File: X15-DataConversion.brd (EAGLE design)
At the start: 24.3 x 25.4 mm, 26 parts, among them Y1 ECS-80-18-4X

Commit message: alumni review changes
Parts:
- removed D1: Green, SparkFun-LED:LED-0603
- removed D3: Orange, SparkFun-LED:LED-0603
- added LED1, LED2: LSM0805452VLED_05452V_VCC, X15-Data-Conversion-Parts:LED_05452V_VCC
- moved R6 0.25 mm to (6.38, 15.4)
- moved R7 0.24 mm to (4.90, 15.4)
- moved U$1 0.09 mm to (8.84, 21.4)
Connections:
- net GND: now also LED1.2, LED2.2; no longer D1.C, D3.C
- net N$1: now also LED1.1; no longer D3.A
- net N$11: now also LED2.1; no longer D1.A
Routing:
- net GND: track 2.83 -> 19.1 mm, vias 6 -> 8
- net 3V3: track 62.8 -> 63.5 mm

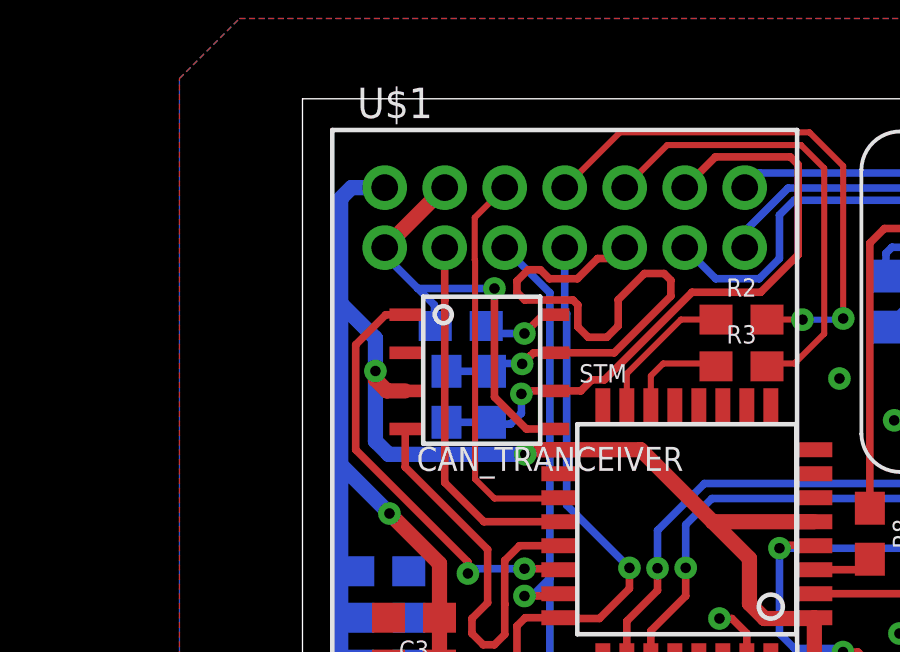
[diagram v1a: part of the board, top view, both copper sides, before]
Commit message: fixed drc error
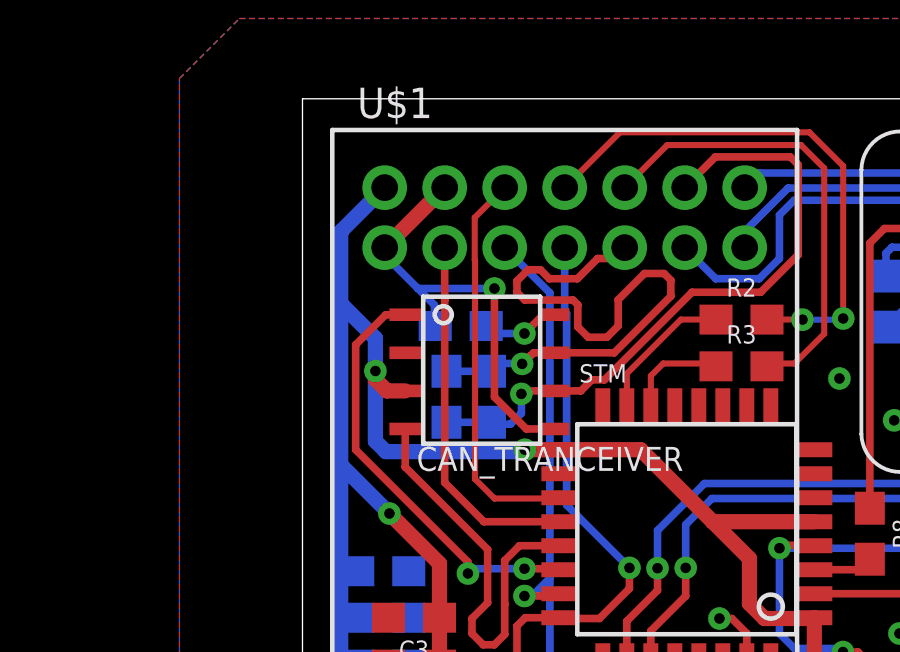
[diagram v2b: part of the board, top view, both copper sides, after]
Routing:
- net 3V3: track 63.5 -> 62.8 mm
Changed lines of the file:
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@@
 <wire x1="8.663" y1="13.626" x2="11.374" y2="13.626" width="0.508" layer="1"/>
 <wire x1="13.774" y1="11.226" x2="17.163" y2="11.226" width="0.508" layer="1"/>
-<via x="7.52749375" y="13.47250625" extent="1-16" drill="0.35"/>
+<via x="7.51479375" y="13.62490625" extent="1-16" drill="0.35"/>
 <wire x1="17.163" y1="8.026" x2="17.163" y2="5.25325" width="0.508" layer="1"/>
 <wire x1="17.415" y1="5.00125" x2="17.163" y2="5.25325" width="0.508" layer="1"/>
-<wire x1="7.52749375" y1="13.47250625" x2="7.6809875" y2="13.626" width="0.508" layer="1"/>
-<wire x1="7.6809875" y1="13.626" x2="8.663" y2="13.626" width="0.508" layer="1"/>
+<wire x1="7.51479375" y1="13.62490625" x2="7.5158875" y2="13.626" width="0.508" layer="1"/>
+<wire x1="7.5158875" y1="13.626" x2="8.663" y2="13.626" width="0.508" layer="1"/>
 <wire x1="1.375" y1="9.5" x2="1.375" y2="8.125" width="0.508" layer="16"/>
 <wire x1="1.375" y1="8.125" x2="1.375" y2="6.625" width="0.508" layer="16"/>
@@
 <via x="3" y="11.5" extent="1-16" drill="0.35"/>
 <wire x1="3" y1="11.5" x2="1.375" y2="13.125" width="0.508" layer="16"/>
-<wire x1="1.375" y1="13.125" x2="1.375" y2="18.5" width="0.508" layer="16"/>
-<wire x1="1.3741375" y1="22.0025375" x2="1.3741375" y2="18.5008625" width="0.508" layer="16"/>
 <wire x1="17.163" y1="8.026" x2="17.137" y2="8" width="0.508" layer="1"/>
 <wire x1="17.137" y1="8" x2="15.5" y2="8" width="0.508" layer="1"/>
@@
 <wire x1="15" y1="8.5" x2="15" y2="10" width="0.508" layer="1"/>
 <wire x1="15" y1="10" x2="13.774" y2="11.226" width="0.508" layer="1"/>
-<wire x1="7.52749375" y1="13.47250625" x2="2.97250625" y2="13.47250625" width="0.508" layer="16"/>
+<wire x1="7.51479375" y1="13.62490625" x2="7.45129375" y2="13.56140625" width="0.508" layer="16"/>
+<wire x1="7.45129375" y1="13.56140625" x2="2.88360625" y2="13.56140625" width="0.508" layer="16"/>
 <wire x1="2.5326" y1="16.25" x2="2.5326" y2="17.3424" width="0.508" layer="16"/>
-<wire x1="2.5326" y1="17.3424" x2="1.375" y2="18.5" width="0.508" layer="16"/>
-<wire x1="1.375" y1="18.5" x2="1.3741375" y2="18.5008625" width="0.508" layer="16"/>
 <wire x1="2.5326" y1="15.9674" x2="2.5326" y2="16.25" width="0.508" layer="1"/>
 <via x="2.5326" y="16.25" extent="1-16" drill="0.35"/>
-<wire x1="2.97250625" y1="13.47250625" x2="2.5326" y2="13.9124125" width="0.508" layer="16"/>
+<wire x1="2.88360625" y1="13.56140625" x2="2.5326" y2="13.9124125" width="0.508" layer="16"/>
 <wire x1="2.5326" y1="13.9124125" x2="2.5326" y2="16.25" width="0.508" layer="16"/>
 <wire x1="3.525" y1="15.587" x2="2.913" y2="15.587" width="0.508" layer="1"/>
 <wire x1="2.913" y1="15.587" x2="2.5326" y2="15.9674" width="0.508" layer="1"/>
-<wire x1="2.8419" y1="22.3627" x2="1.7343" y2="22.3627" width="0.508" layer="16"/>
-<wire x1="1.7343" y1="22.3627" x2="1.3741375" y2="22.0025375" width="0.508" layer="16"/>
+<wire x1="2.8419" y1="22.3627" x2="1.375" y2="20.8958" width="0.508" layer="16"/>
+<wire x1="1.375" y1="20.8958" x2="1.375" y2="18.5" width="0.508" layer="16"/>
+<wire x1="1.375" y1="18.5" x2="1.375" y2="13.125" width="0.508" layer="16"/>
+<wire x1="2.5326" y1="17.3424" x2="1.375" y2="18.5" width="0.508" layer="16"/>
 </signal>
 <signal name="ALERT1">

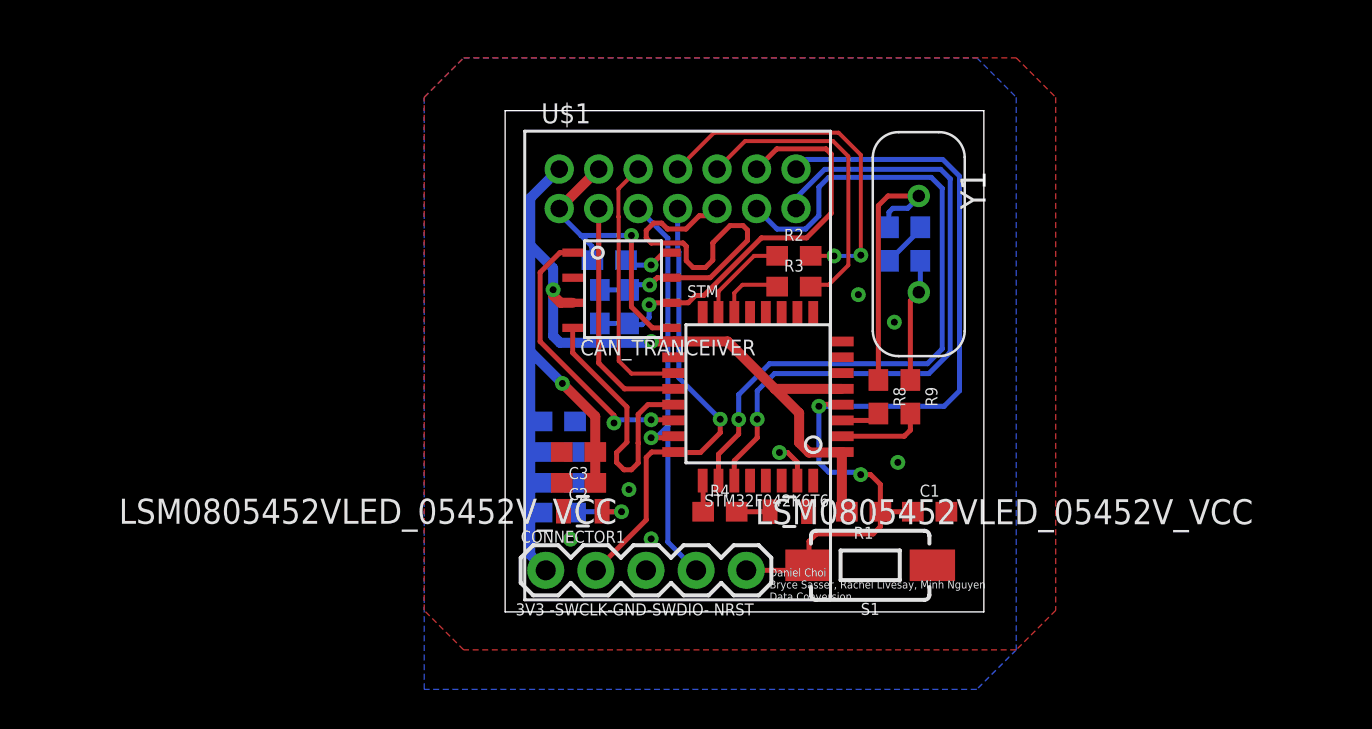
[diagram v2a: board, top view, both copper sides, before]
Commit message: removed oscillator and fixed trace widths
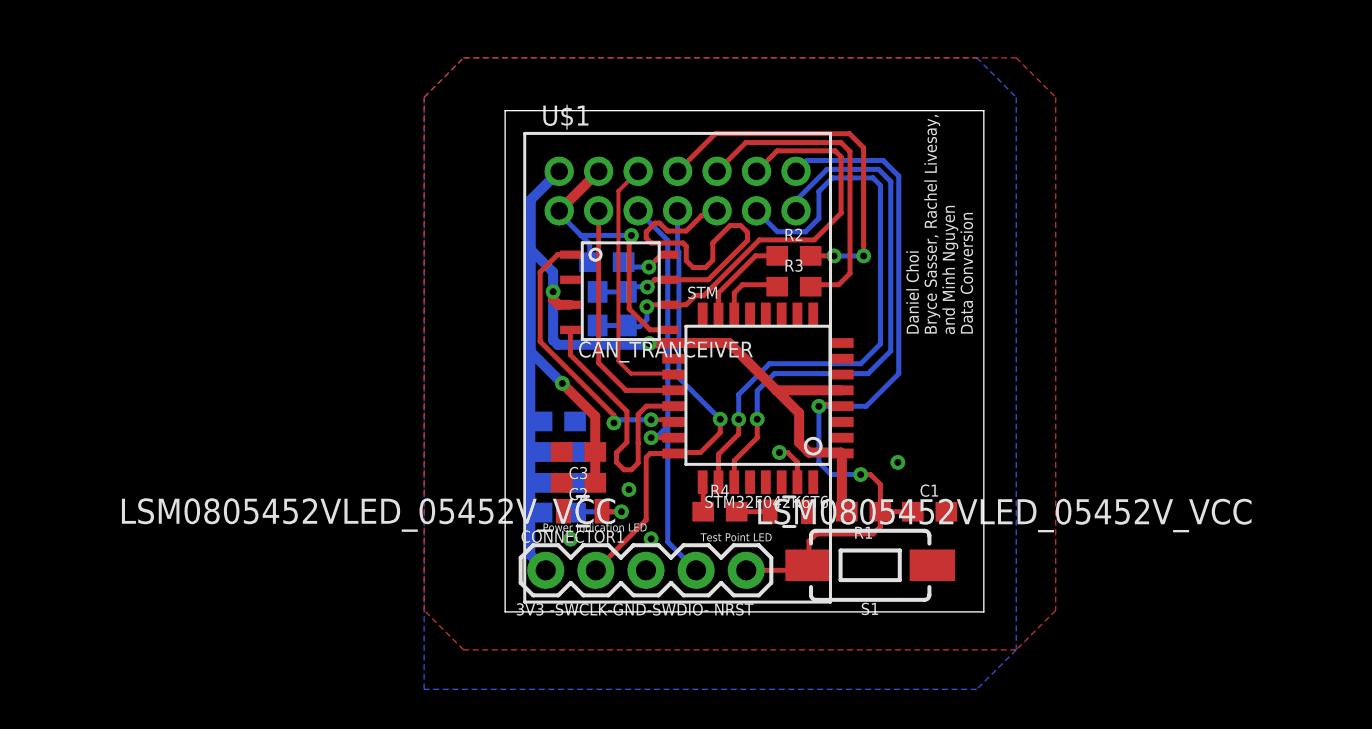
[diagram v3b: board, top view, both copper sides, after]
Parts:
- removed C7, C8: 18pF, SparkFun-RF:0603
- removed R8, R9: 0, SparkFun-Resistors:0603
- removed Y1: ECS-80-18-4X, X15-Data-Conversion-Parts:XTAL_ECS-80-18-4X
- moved R10 0.15 mm to (5.26, 17.6)
- moved R6 0.15 mm to (6.27, 15.3)
- moved R7 0.15 mm to (4.79, 15.3)
- moved CAN_TRANCEIVER 0.15 mm to (3.41, 18.0)
- moved U$1 0.11 mm to (8.84, 21.2)
- moved STM 0.08 mm to (15.7, 15.0)
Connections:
- removed net N$3: C7.1, R8.1, Y1.1
- removed net N$4: C8.1, R9.1, Y1.2
- net GND: no longer C7.2, C8.2
- net OSC_IN: no longer R9.2
- net OSC_OUT: no longer R8.2
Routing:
- net N$3: track 13.7 -> 0.00 mm
- net NRST: track 47.0 -> 40.4 mm
- net N$4: track 6.25 -> 0.00 mm
- net ALERT2: track 36.2 -> 30.0 mm
- net ALERT1: track 33.6 -> 27.5 mm
- net OSC_IN: track 4.44 -> 0.00 mm
- net GND: track 19.1 -> 16.9 mm, vias 8 -> 6
- net OSC_OUT: track 2.00 -> 0.00 mm
- net CAN_L: track 21.9 -> 22.9 mm
- net C2_1: track 15.4 -> 16.0 mm
- net C2_2: track 18.2 -> 18.7 mm
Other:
- board text added: "Daniel Choi Bryce Sasser, Rachel Livesay, and Minh Nguyen Data Conversion"
- board text added: "Power Indication LED"
- board text added: "Test Point LED"
- board text removed: "Daniel Choi Bryce Sasser, Rachel Livesay, Minh Nguyen Data Conversion"

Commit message: added 5 pin connector
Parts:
- added U$2: STM_CONN, X15-Data-Conversion-Parts:1X05
- moved R3 0.10 mm to (14.7, 16.5), flipped to the bottom, turned to 180 degrees
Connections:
- new net ADC_IN0: STM.PA5, U$2.1
- new net ADC_IN1: STM.PA4, U$2.2
- new net ADC_IN2: STM.PA6, U$2.3
- net 3V3: now also U$2.4
- net GND: now also U$2.5
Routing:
- net ADC_IN2: track 0.00 -> 10.8 mm
- net ADC_IN0: track 0.00 -> 9.61 mm
- net ADC_IN1: track 0.00 -> 8.30 mm
- net 3V3: track 62.4 -> 67.8 mm
- net C2_1: track 16.0 -> 15.8 mm, vias 0 -> 1
- net N$7: vias 0 -> 1
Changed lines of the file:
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@@
 <wire x1="24.3586" y1="25.3238" x2="0.1016" y2="25.3238" width="0" layer="20"/>
 <wire x1="0.1016" y1="25.3238" x2="0.1016" y2="-0.0762" width="0" layer="20"/>
-<text x="23.8031" y="13.9525" size="0.6096" layer="21" rot="R90">Daniel Choi
-Bryce Sasser, Rachel Livesay,
+<text x="23.8031" y="18.9525" size="0.508" layer="21" rot="R90">Daniel Choi
+Bryce Sasser,
+Rachel Livesay,
 and Minh Nguyen
 Data Conversion</text>
@@
 <attribute name="VALUE" x="14.515" y="17.203" size="0.6096" layer="28" font="vector" ratio="20" rot="MR0" align="top-center"/>
 </element>
-<element name="R3" library="SparkFun-Resistors" package="0603" value="4.7k" x="14.735" y="16.405" smashed="yes">
-<attribute name="NAME" x="14.735" y="17.167" size="0.6096" layer="25" font="vector" ratio="20" align="bottom-center"/>
-<attribute name="PROD_ID" value=" " x="14.735" y="16.405" size="1.778" layer="27" display="off"/>
-<attribute name="VALUE" x="14.735" y="15.643" size="0.6096" layer="27" font="vector" ratio="20" align="top-center"/>
+<element name="R3" library="SparkFun-Resistors" package="0603" value="4.7k" x="14.7223" y="16.5007" smashed="yes" rot="MR180">
+<attribute name="NAME" x="14.7223" y="15.7387" size="0.6096" layer="26" font="vector" ratio="20" rot="MR180" align="bottom-center"/>
+<attribute name="PROD_ID" value=" " x="14.7223" y="16.5007" size="1.778" layer="28" rot="MR180" display="off"/>
+<attribute name="VALUE" x="14.7223" y="17.2627" size="0.6096" layer="28" font="vector" ratio="20" rot="MR180" align="top-center"/>
 </element>
 <element name="R4" library="SparkFun-Resistors" package="0603" value="470" x="10.985" y="5.00125" smashed="yes">
@@
 <attribute name="PROD_ID" value=" " x="4.788" y="15.2886" size="1.778" layer="28" rot="MR90" display="off"/>
 <attribute name="VALUE" x="4.026" y="15.2886" size="0.6096" layer="28" font="vector" ratio="20" rot="MR90" align="top-center"/>
+</element>
+<element name="U$2" library="X15-Data-Conversion-Parts" package="1X05" package3d_urn="urn:adsk.eagle:package:38192072/1" value="STM_CONN" x="22.012" y="17.6251" smashed="yes" rot="R270">
+<attribute name="NAME" x="23.409" y="18.8951" size="0.6096" layer="25" font="vector" ratio="20" rot="R270"/>
+<attribute name="VALUE" x="19.726" y="19.1491" size="0.6096" layer="25" rot="R270"/>
 </element>
 </elements>
@@
 <wire x1="3.9489" y1="19" x2="6.5" y2="19" width="0.254" layer="16"/>
 <via x="6.5" y="19" extent="1-16" drill="0.35"/>
-<wire x1="6.5" y1="19" x2="6.3857" y2="18.8857" width="0.254" layer="1"/>
-<wire x1="6.3857" y1="18.8857" x2="6.3857" y2="15.2805" width="0.254" layer="1"/>
+<wire x1="6.5" y1="19" x2="6.5" y2="15.1662" width="0.254" layer="1"/>
 <wire x1="7.4508" y1="14.2154" x2="8.3607" y2="14.2154" width="0.254" layer="1"/>
 <wire x1="2.8419" y1="20.107" x2="3.9489" y2="19" width="0.254" layer="16"/>
-<wire x1="6.3857" y1="15.2805" x2="7.4508" y2="14.2154" width="0.254" layer="1"/>
+<wire x1="6.5" y1="15.1662" x2="7.4508" y2="14.2154" width="0.254" layer="1"/>
 <wire x1="4.3857" y1="18.5632" x2="3.9489" y2="19" width="0.254" layer="16"/>
 <wire x1="4.3857" y1="17.6734" x2="4.3857" y2="18.5632" width="0.254" layer="16"/>
+<contactref element="U$2" pad="5"/>
 </signal>
 <signal name="NRST">
@@
 <contactref element="STM" pad="PB0"/>
 <contactref element="R3" pad="1"/>
-<wire x1="13.885" y1="16.405" x2="13.79" y2="16.5" width="0.2032" layer="1"/>
-<wire x1="13.79" y1="16.5" x2="12.125" y2="16.5" width="0.254" layer="1"/>
+<wire x1="13.79" y1="16.5" x2="13.8723" y2="16.5007" width="0.2032" layer="16"/>
 <wire x1="11.713" y1="16.088" x2="11.713" y2="14.9998" width="0.254" layer="1"/>
-<wire x1="12.125" y1="16.5" x2="11.713" y2="16.088" width="0.254" layer="1"/>
+<wire x1="11.713" y1="16.088" x2="12.125" y2="16.5" width="0.254" layer="1"/>
+<wire x1="12.125" y1="16.5" x2="12.19059375" y2="16.43440625" width="0.254" layer="1"/>
+<via x="12.19059375" y="16.43440625" extent="1-16" drill="0.35"/>
+<wire x1="12.19059375" y1="16.43440625" x2="12.2561875" y2="16.5" width="0.254" layer="16"/>
+<wire x1="12.2561875" y1="16.5" x2="13.79" y2="16.5" width="0.254" layer="16"/>
 </signal>
 <signal name="C2_2">
@@
 <wire x1="10.8419" y1="22.2484" x2="12.2981" y2="23.7046" width="0.254" layer="1"/>
 <wire x1="17.12123125" y1="23.7046" x2="12.2981" y2="23.7046" width="0.254" layer="1"/>
-<wire x1="15.585" y1="16.405" x2="15.68" y2="16.5" width="0.254" layer="1"/>
-<wire x1="15.68" y1="16.5" x2="17" y2="16.5" width="0.254" layer="1"/>
-<wire x1="17" y1="16.5" x2="17.5768" y2="17.0768" width="0.254" layer="1"/>
-<wire x1="17.5768" y1="17.0768" x2="17.5768" y2="23.24903125" width="0.254" layer="1"/>
+<wire x1="17.5768" y1="17.2546" x2="17.5588" y2="17.2366" width="0.254" layer="1"/>
+<wire x1="17.5768" y1="17.2546" x2="17.5768" y2="23.24903125" width="0.254" layer="1"/>
 <wire x1="17.5768" y1="23.24903125" x2="17.12123125" y2="23.7046" width="0.254" layer="1"/>
+<via x="17.5588" y="17.2366" extent="1-16" drill="0.35"/>
+<wire x1="17.0896" y1="16.7674" x2="15.839" y2="16.7674" width="0.254" layer="16"/>
+<wire x1="15.5723" y1="16.5007" x2="15.839" y2="16.7674" width="0.254" layer="16"/>
+<wire x1="17.0896" y1="16.7674" x2="17.5588" y2="17.2366" width="0.254" layer="16"/>
 </signal>
 <signal name="LED">
@@
 <wire x1="1.4004" y1="18.2714" x2="1.4004" y2="13.0996" width="0.508" layer="16"/>
 <wire x1="2.5326" y1="17.1392" x2="1.4004" y2="18.2714" width="0.508" layer="16"/>
+<contactref element="U$2" pad="4"/>
+<wire x1="17.163" y1="11.1498" x2="18.8502" y2="11.1498" width="0.508" layer="1"/>
+<wire x1="18.8502" y1="11.1498" x2="20" y2="10" width="0.508" layer="1"/>
+<wire x1="20" y1="10" x2="22.0069" y2="10" width="0.508" layer="1"/>
+<wire x1="22.0069" y1="10" x2="22.012" y2="10.0051" width="0.508" layer="1"/>
 </signal>
 <signal name="ALERT1">
@@
 <via x="11" y="9.6875" extent="1-16" drill="0.35"/>
 <wire x1="8.7132" y1="8" x2="10" y2="8" width="0.254" layer="1"/>
-<wire x1="8.8419" y1="20.2484" x2="8.8419" y2="18.2328375" width="0.254" layer="16"/>
-<wire x1="8.8419" y1="18.2328375" x2="8.9064" y2="18.1683375" width="0.254" layer="16"/>
-<wire x1="8.9064" y1="11.7811" x2="11" y2="9.6875" width="0.254" layer="16"/>
-<wire x1="8.9064" y1="18.1683375" x2="8.9064" y2="11.7811" width="0.254" layer="16"/>
+<wire x1="8.8419" y1="20.2484" x2="8.8419" y2="18.2201375" width="0.254" layer="16"/>
+<wire x1="8.8419" y1="18.2201375" x2="8.8429" y2="18.2191375" width="0.254" layer="16"/>
+<wire x1="8.8429" y1="11.8446" x2="11" y2="9.6875" width="0.254" layer="16"/>
+<wire x1="8.8429" y1="18.2191375" x2="8.8429" y2="11.8446" width="0.254" layer="16"/>
 </signal>
 <signal name="SWDIO">
@@
 <wire x1="1.875" y1="17.1377" x2="2.7607" y2="18.0234" width="0.254" layer="1"/>
 <wire x1="2.7607" y1="18.0234" x2="3.4087" y2="18.0234" width="0.254" layer="1"/>
-<wire x1="1.875" y1="17.1377" x2="1.875" y2="13.625" width="0.254" layer="1"/>
+<wire x1="1.875" y1="17.1377" x2="1.875" y2="13.5869" width="0.254" layer="1"/>
 <via x="7.5" y="9.6588" extent="1-16" drill="0.35"/>
 <wire x1="7.5" y1="9.6588" x2="8.6282" y2="9.6588" width="0.254" layer="1"/>
 <wire x1="8.6282" y1="9.6588" x2="8.7001" y2="9.5869" width="0.254" layer="1"/>
-<wire x1="5.6156" y1="9.8844" x2="5.6156" y2="9.5" width="0.254" layer="1"/>
-<via x="5.6156" y="9.5" extent="1-16" drill="0.35"/>
-<wire x1="5.6156" y1="9.5" x2="5.7744" y2="9.6588" width="0.254" layer="16"/>
-<wire x1="5.7744" y1="9.6588" x2="7.5" y2="9.6588" width="0.254" layer="16"/>
-<wire x1="1.875" y1="13.625" x2="5.6156" y2="9.8844" width="0.254" layer="1"/>
+<wire x1="5.6156" y1="9.8463" x2="5.6156" y2="9.7574" width="0.254" layer="1"/>
+<wire x1="5.6156" y1="9.8463" x2="1.875" y2="13.5869" width="0.254" layer="1"/>
+<via x="5.6156" y="9.7574" extent="1-16" drill="0.35"/>
+<wire x1="5.6156" y1="9.7574" x2="7.4014" y2="9.7574" width="0.254" layer="16"/>
+<wire x1="7.4014" y1="9.7574" x2="7.5" y2="9.6588" width="0.254" layer="16"/>
 </signal>
 <signal name="CAN_RX">
@@
 <wire x1="7.3857" y1="17.3984" x2="6.3607" y2="17.3984" width="0.254" layer="16"/>
 </signal>
+<signal name="ADC_IN0">
+<contactref element="U$2" pad="1"/>
+<contactref element="STM" pad="PA5"/>
+<wire x1="22.012" y1="17.6251" x2="18.8772875" y2="17.6251" width="0.254" layer="1"/>
+<wire x1="14.113" y1="16.0688" x2="14.113" y2="14.9998" width="0.254" layer="1"/>
+<wire x1="18.8772875" y1="17.6251" x2="17.6251875" y2="16.373" width="0.254" layer="1"/>
+<wire x1="17.6251875" y1="16.373" x2="14.4172" y2="16.373" width="0.254" layer="1"/>
+<wire x1="14.4172" y1="16.373" x2="14.113" y2="16.0688" width="0.254" layer="1"/>
+</signal>
+<signal name="ADC_IN1">
+<contactref element="U$2" pad="2"/>
+<contactref element="STM" pad="PA4"/>
+<wire x1="14.913" y1="14.9998" x2="14.913" y2="15.7733" width="0.254" layer="1"/>
+<wire x1="14.913" y1="15.7733" x2="15.0889" y2="15.9492" width="0.254" layer="1"/>
+<wire x1="15.0889" y1="15.9492" x2="21.1479" y2="15.9492" width="0.254" layer="1"/>
+<wire x1="21.1479" y1="15.9492" x2="22.012" y2="15.0851" width="0.254" layer="1"/>
+</signal>
+<signal name="ADC_IN2">
+<contactref element="STM" pad="PA6"/>
+<contactref element="U$2" pad="3"/>
+<wire x1="13.313" y1="14.9998" x2="13.313" y2="13.9537" width="0.254" layer="1"/>
+<wire x1="13.313" y1="13.9537" x2="13.7667" y2="13.5" width="0.254" layer="1"/>
+<wire x1="13.7667" y1="13.5" x2="15.8556" y2="13.5" width="0.254" layer="1"/>
+<wire x1="15.8556" y1="13.5" x2="16.4653" y2="14.1097" width="0.254" layer="1"/>
+<wire x1="22.012" y1="12.5451" x2="20.4474" y2="14.1097" width="0.254" layer="1"/>
+<wire x1="20.4474" y1="14.1097" x2="16.4653" y2="14.1097" width="0.254" layer="1"/>
+</signal>
 </signals>
